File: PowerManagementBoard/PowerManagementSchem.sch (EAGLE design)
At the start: 95 parts, among them J1 D15S24A4GV00LF, U1 VX7805-500, U2 PYB20-Q24-S5, U3 PYB30-Q48-S5, U4 PYB30-Q48-S12, U5 3V3REG, U6 INA4180-SPLIT, U7 INA4180-SPLIT, U8 TEENSY-4.0SILK, U9 INA4180-SPLIT

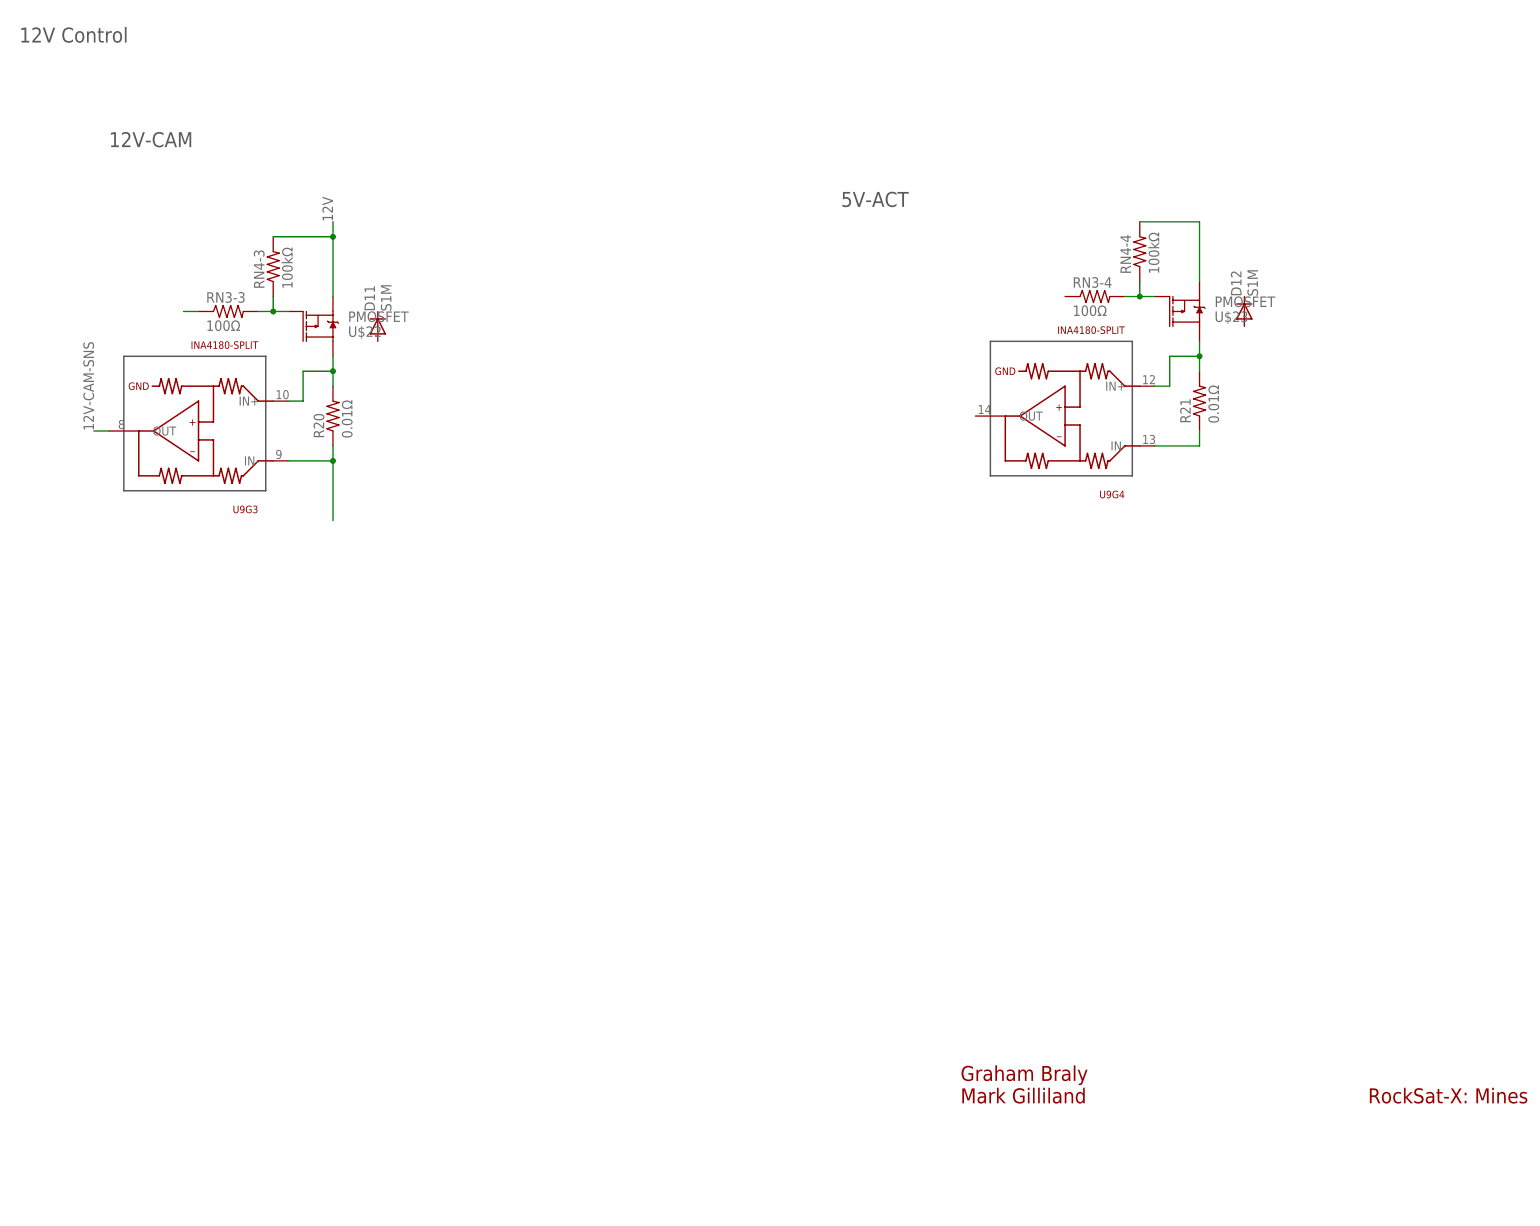
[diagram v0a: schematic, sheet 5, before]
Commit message: Added useless LED for test, names some nets.
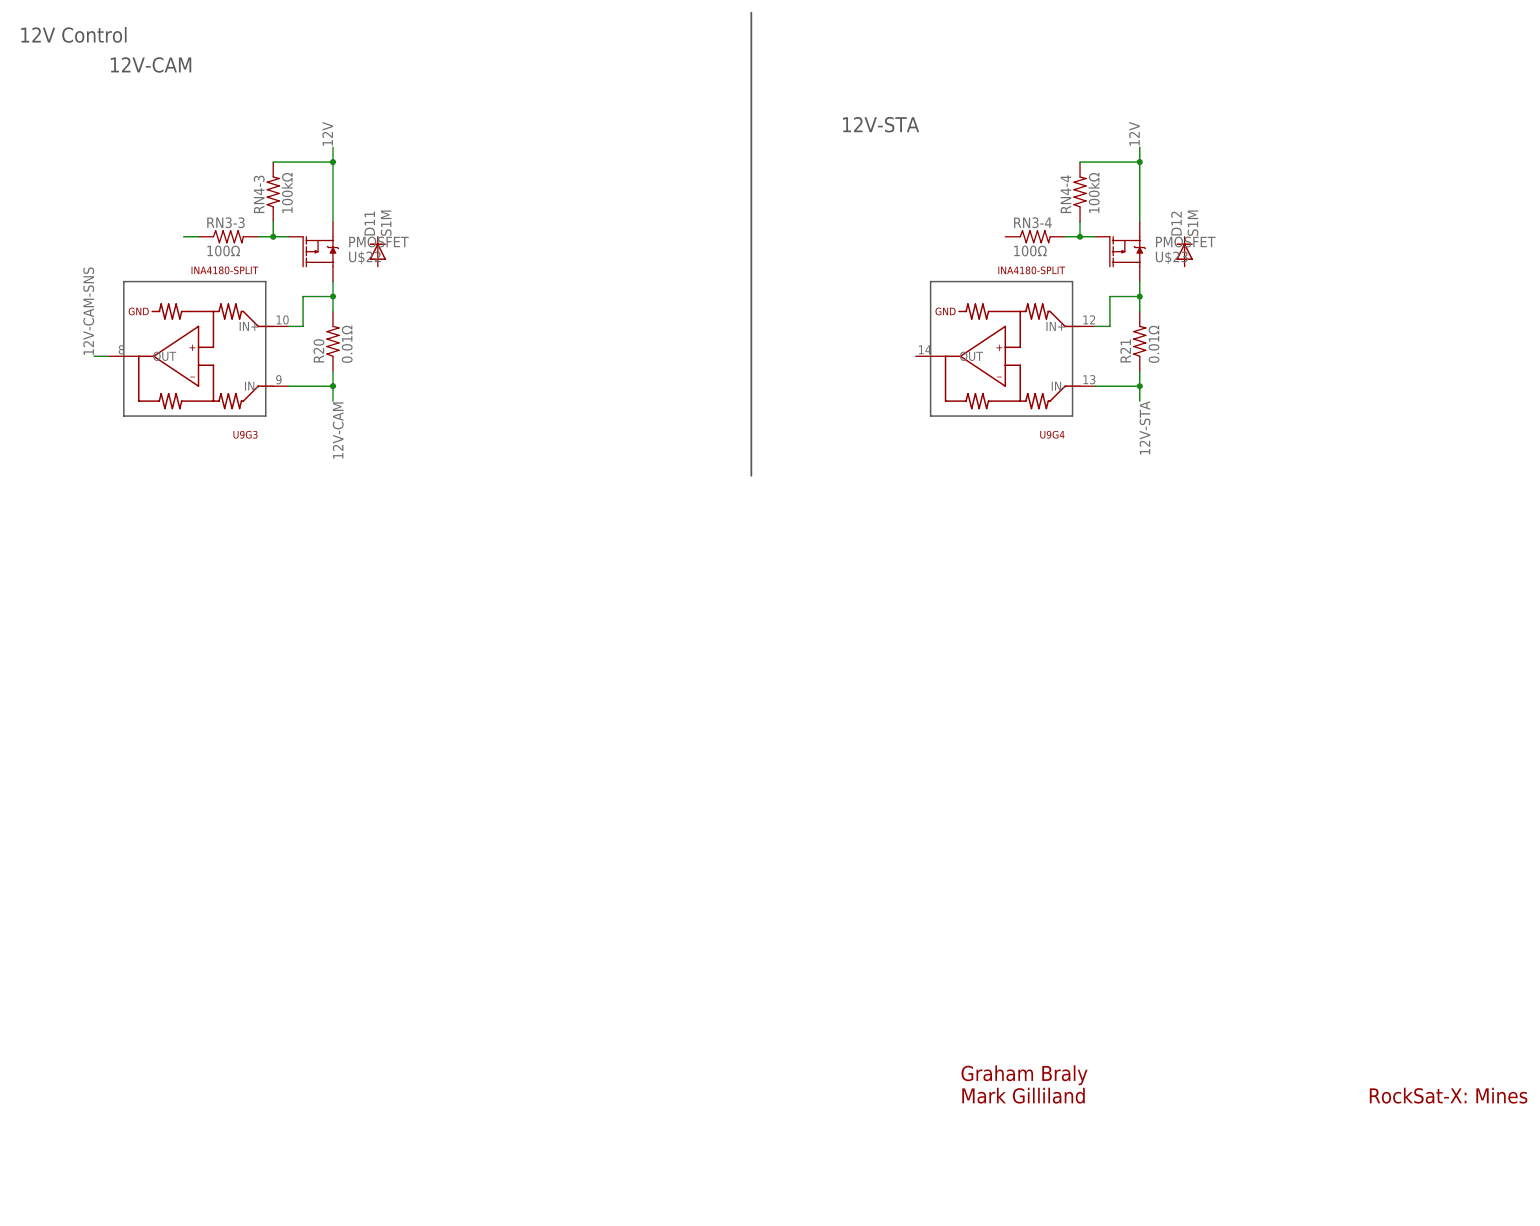
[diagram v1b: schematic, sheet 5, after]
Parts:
- added U$25: FLAT_LED, PowerManagementParts:FLAT_LED
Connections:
- removed net N$35: R20.1, U9G3.IN-
- removed net N$37: R21.1, U9G4.IN-
- removed net N$42: RN4-4.2, U$23.S
- net 12V: now also RN4-4.2, U$23.S
- net 12V-CAM: now also R20.1, U9G3.IN-
- net 12V-STA: now also R21.1, U9G4.IN-
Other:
- note added: "12V-STA"
- moved on the sheet: D11, D12, R20, R21, RN3-3, RN3-4, RN4-3, RN4-4, U$22, U$23, U9G3, U9G4

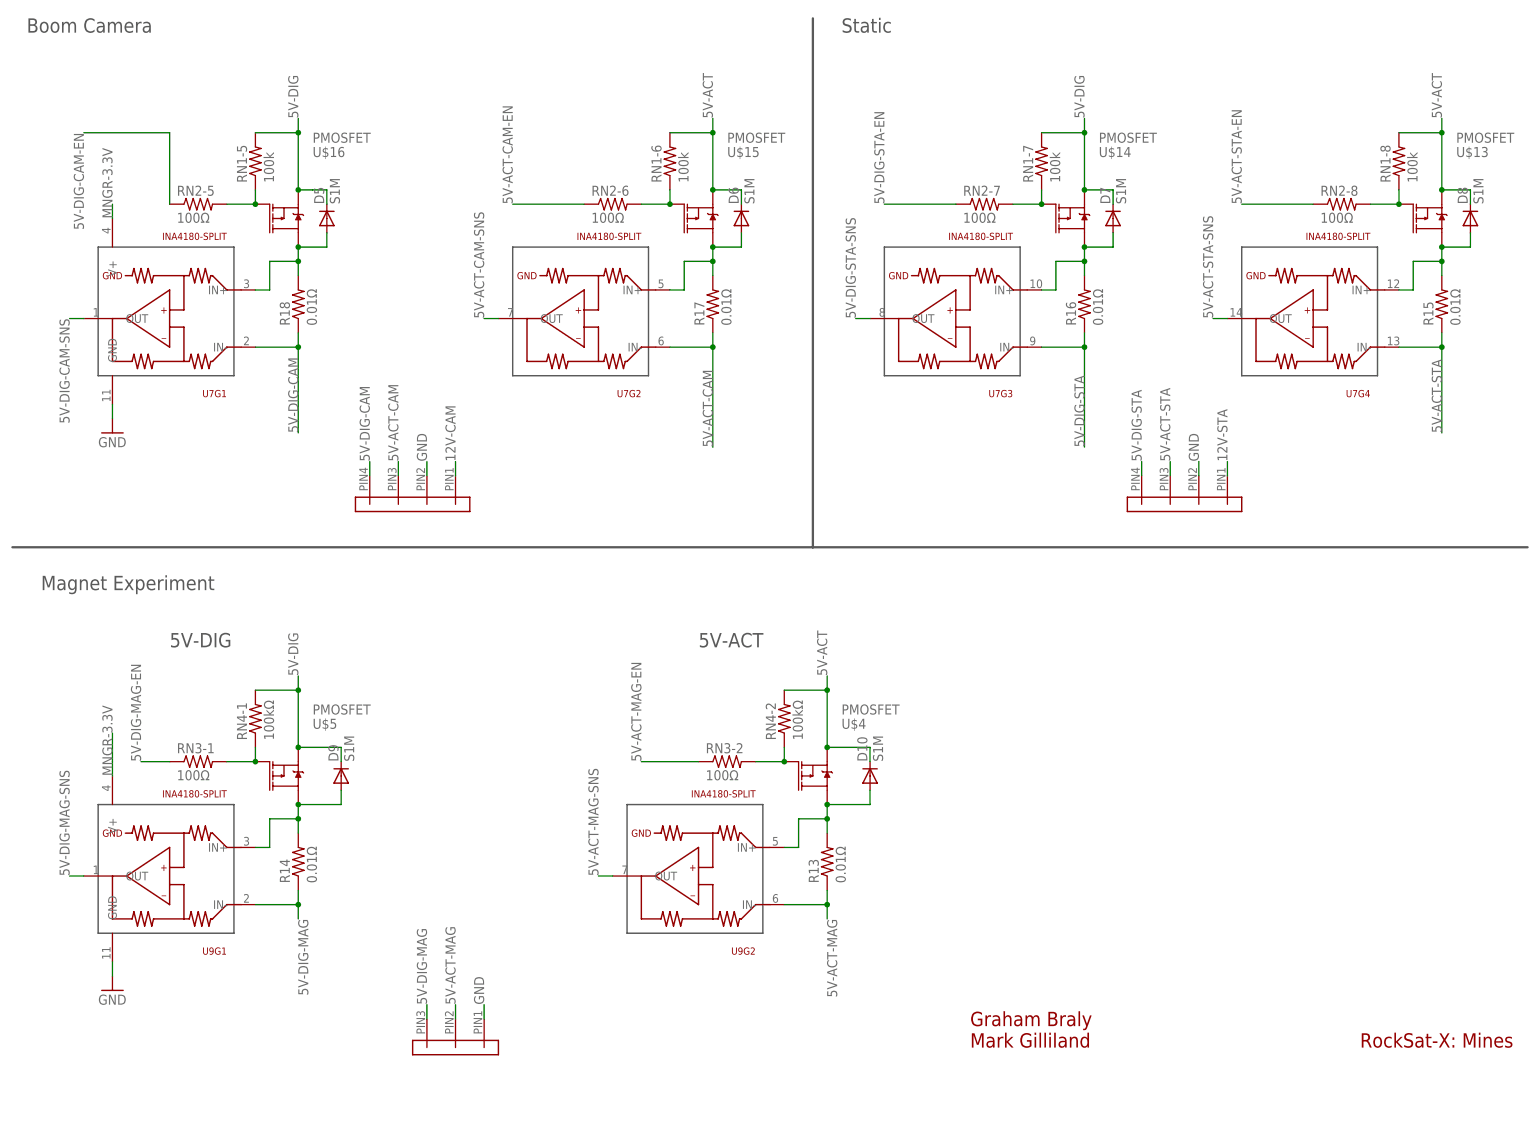
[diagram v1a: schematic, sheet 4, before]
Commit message: Finalized schematic. Ready for board layout
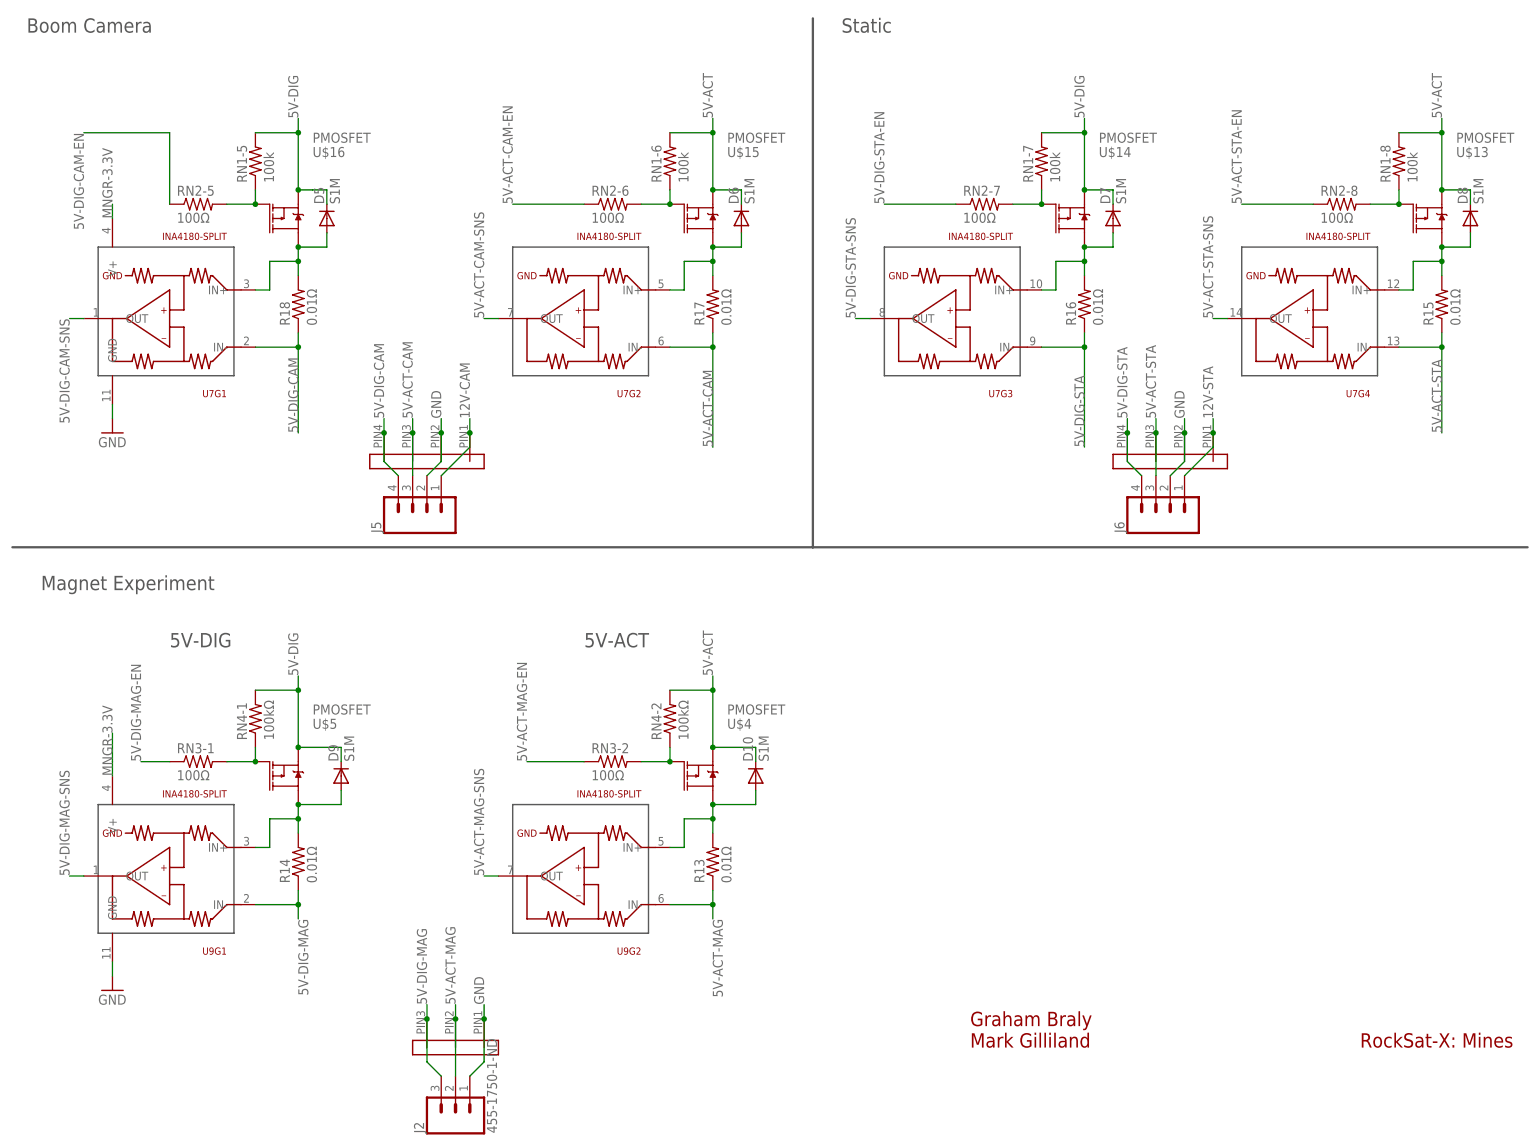
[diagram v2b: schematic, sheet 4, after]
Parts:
- removed U$21, U$25: FLAT_LED, PowerManagementParts:FLAT_LED
- added J2: 455-1750-1-ND, SparkFun-Connectors:CONN_03
- added J3, J4: (no value), SparkFun-Connectors:CONN_03
- added J5, J6: (no value), SparkFun-Connectors:CONN_04PTH
- added J7: (no value), SparkFun-Connectors:CONN_05X2PTH
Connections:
- removed net N$33: RN3-3.1
- net 12V: now also J7.10
- net 12V-CAM: now also J5.1
- net 12V-CAM-EN: now also RN3-3.1
- net 12V-STA: now also J6.1
- net 12V-STA-EN: now also RN3-4.1
- net 12V-STA-SNS: now also U9G4.OUT
- net 5V-ACT: now also J7.8
- net 5V-ACT-CAM: now also J5.3
- net 5V-ACT-LASER: now also J4.2
- net 5V-ACT-MAG: now also J2.2
- net 5V-ACT-STA: now also J6.3
- net 5V-ACT-TX: now also J3.2
- net 5V-DIG: now also J7.6
- net 5V-DIG-CAM: now also J5.4
- net 5V-DIG-LASER: now also J4.3
- net 5V-DIG-MAG: now also J2.3
- net 5V-DIG-STA: now also J6.4
- net 5V-DIG-TX: now also J3.3
- net GND: now also J2.1, J3.1, J4.1, J5.2, J6.2, J7.1
- net MNGR-3.3V: now also J7.4, U$20.ANODE
- net MNGR-5V: now also J7.2; no longer U$20.ANODE
- net SUPPLY_FOR_12V: now also J7.7
- net SUPPLY_FOR_5V-ACT: now also J7.5
- net SUPPLY_FOR_5V-DIG: now also J7.3
- net SUPPLY_FOR_MNGR: now also J7.9
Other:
- note removed: "add connections"
- note removed: "add test points"
- note removed: "test for git"
- moved on the sheet: D10, R13, RN3-2, RN4-2, U$4, U9G2

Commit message: Initial board layout
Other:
- moved on the sheet: D11, D12
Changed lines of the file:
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@@
 <attribute name="VALUE" x="71.882" y="151.13" size="1.778" layer="96" rot="R90"/>
 </instance>
-<instance part="D11" gate="G$1" x="76.2" y="170.18" rot="R90"/>
+<instance part="D11" gate="G$1" x="83.82" y="170.18" rot="R90"/>
 <instance part="U$23" gate="G$1" x="203.2" y="170.18" smashed="yes" rot="MR180">
 <attribute name="NAME" x="208.28" y="170.18" size="1.778" layer="95" font="vector" rot="MR180"/>
@@
 <attribute name="VALUE" x="209.042" y="151.13" size="1.778" layer="96" rot="R90"/>
 </instance>
-<instance part="D12" gate="G$1" x="213.36" y="170.18" rot="R90"/>
+<instance part="D12" gate="G$1" x="220.98" y="170.18" rot="R90"/>
 <instance part="RN4" gate="-3" x="58.42" y="180.34" rot="R90"/>
 <instance part="RN4" gate="-4" x="195.58" y="180.34" rot="R90"/>
